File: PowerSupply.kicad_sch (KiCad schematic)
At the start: 8 parts, among them U1201 TPSM365R6FRDNR

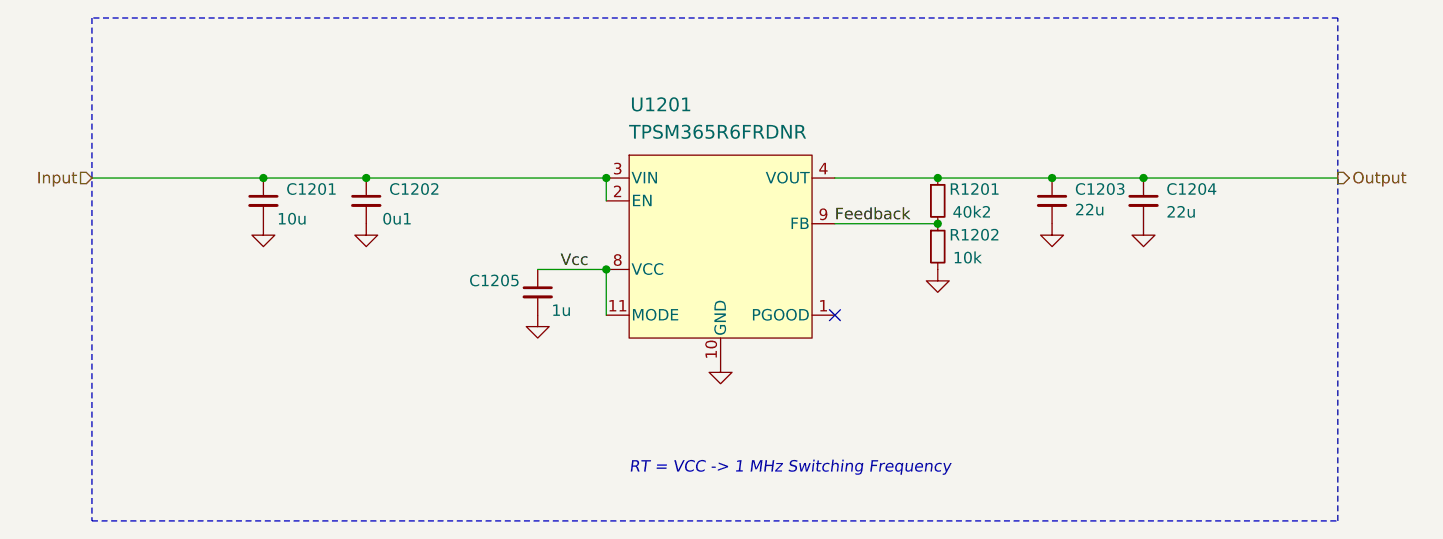
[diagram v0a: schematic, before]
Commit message: Replace step-down
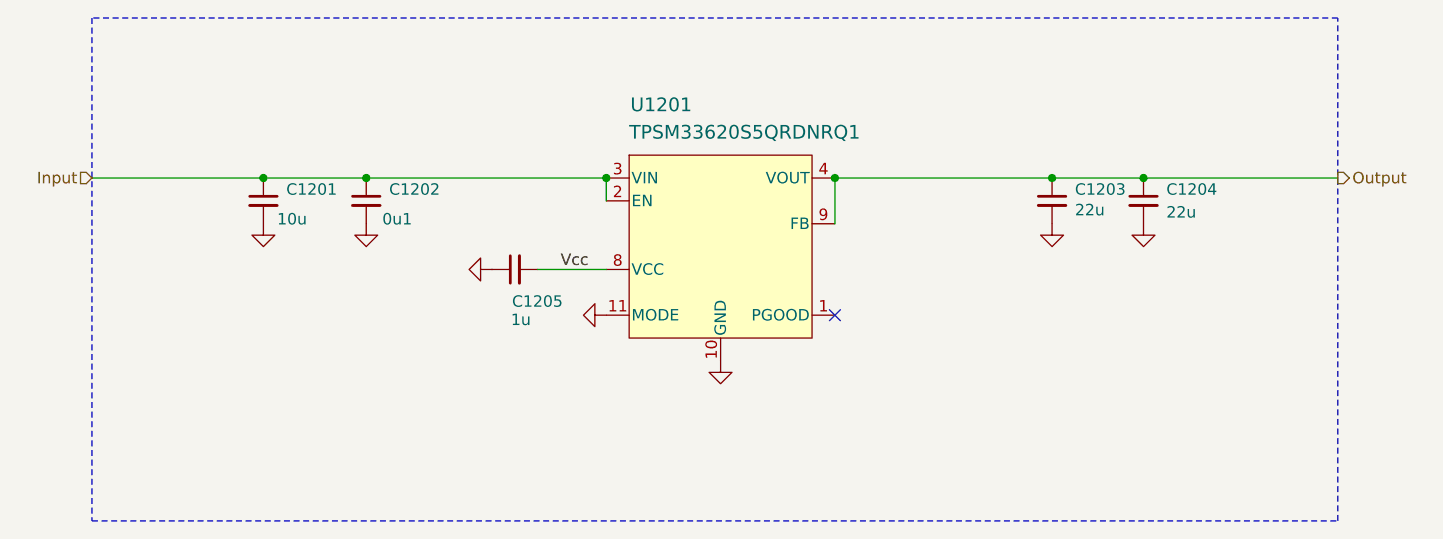
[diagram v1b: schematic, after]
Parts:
- removed R1201: 40k2, V2_Resistor_SMD:R_0603, symbol V2_Resistor:0603_40k2
- removed R1202: 10k, V2_Resistor_SMD:R_0603, symbol V2_Resistor:0603_10k
- U1201: value TPSM365R6FRDNR -> TPSM33620S5QRDNRQ1; symbol V2_Converter_DCDC:TPSM365R6FRDNR -> V2_Converter_DCDC:TPSM33620S5QRDNRQ1; Mouser 595-TPSM365R6FRDNR -> 595-SM33620S5QRDNRQ1; Product TPSM365R6FRDNR -> TPSM33620S5QRDNRQ1; Rating 600mA -> 2A
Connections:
- net Feedback is gone; now on net Output: U1201.9 (FB)
- net GND: now also C1205.1, U1201.11 (MODE); no longer C1205.2
- net Vcc: now also C1205.2; no longer C1205.1, U1201.11 (MODE)
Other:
- note removed: "RT = VCC -> 1 MHz Switching Frequency"
- moved on the sheet: C1205

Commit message: Update
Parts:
- C1201, C1202, C1203, C1204, C1205: Id (none) -> Capacitor:${SYMBOL_NAME}
- U1201: Id (none) -> DCDC:${SYMBOL_NAME}
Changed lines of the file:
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@@
+			)
+		)
+		(property "Id" "DCDC:${SYMBOL_NAME}"
+			(at 148.59 147.32 0)
+			(hide yes)
+			(show_name no)
+			(do_not_autoplace no)
+			(effects
+				(font
+					(size 1.27 1.27)
+				)
 			)
 		)
@@
 			)
 		)
+		(property "Id" "Capacitor:${SYMBOL_NAME}"
+			(at 109.22 113.03 0)
+			(hide yes)
+			(show_name no)
+			(do_not_autoplace no)
+			(effects
+				(font
+					(size 1.27 1.27)
+				)
+			)
+		)
 		(pin "1"
 		)
@@
 			)
 		)
+		(property "Id" "Capacitor:${SYMBOL_NAME}"
+			(at 195.58 113.03 0)
+			(hide yes)
+			(show_name no)
+			(do_not_autoplace no)
+			(effects
+				(font
+					(size 1.27 1.27)
+				)
+			)
+		)
 		(pin "1"
 		)
@@
 			)
 		)
+		(property "Id" "Capacitor:${SYMBOL_NAME}"
+			(at 140.97 105.41 0)
+			(hide yes)
+			(show_name no)
+			(do_not_autoplace no)
+			(effects
+				(font
+					(size 1.27 1.27)
+				)
+			)
+		)
 		(pin "1"
 		)
@@
 			)
 		)
+		(property "Id" "Capacitor:${SYMBOL_NAME}"
+			(at 185.42 113.03 0)
+			(hide yes)
+			(show_name no)
+			(do_not_autoplace no)
+			(effects
+				(font
+					(size 1.27 1.27)
+				)
+			)
+		)
 		(pin "1"
 		)
@@
 			(hide yes)
 			(show_name no)
+			(do_not_autoplace no)
+			(effects
+				(font
+					(size 1.27 1.27)
+				)
+			)
+		)
+		(property "Id" "Capacitor:${SYMBOL_NAME}"
+			(at 97.79 113.03 0)
+			(hide yes)
+			(show_name no)

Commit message: Update
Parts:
- renumbered C1201 to C601, C1202 to C602, C1205 to C603, C1203 to C604, C1204 to C605, U1201 to U601
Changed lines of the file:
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@@
 		(rev "2026-03-28")
 		(company "Versio Duo")
+		(comment 1 "V2 Link Connector")
 	)
 	(junction
@@
 		(in_pos_files yes)
 		(dnp no)
-		(property "Reference" "U1201"
+		(property "Reference" "U601"
 			(at 141.986 87.122 0)
 			(show_name no)
@@
 			(project "connect"
 				(path "/6c8448b4-b04d-47e1-934e-e40cbe27a7be/095cddf1-6522-4d3b-885d-b21acd91d0c6"
-					(reference "U1201")
+					(reference "U601")
 					(unit 1)
 				)
@@
 		(in_pos_files yes)
 		(dnp no)
-		(property "Reference" "C1202"
+		(property "Reference" "C602"
 			(at 111.76 96.52 0)
 			(show_name no)
@@
 			(project "connect"
 				(path "/6c8448b4-b04d-47e1-934e-e40cbe27a7be/095cddf1-6522-4d3b-885d-b21acd91d0c6"
-					(reference "C1202")
+					(reference "C602")
 					(unit 1)
 				)
@@
 		(in_pos_files yes)
 		(dnp no)
-		(property "Reference" "C1204"
+		(property "Reference" "C605"
 			(at 198.12 96.52 0)
 			(show_name no)
@@
 			(project "connect"
 				(path "/6c8448b4-b04d-47e1-934e-e40cbe27a7be/095cddf1-6522-4d3b-885d-b21acd91d0c6"
-					(reference "C1204")
+					(reference "C605")
 					(unit 1)
 				)
@@
 		(in_pos_files yes)
 		(dnp no)
-		(property "Reference" "#PWR1203"
+		(property "Reference" "#PWR0606"
 			(at 185.42 106.68 0)
 			(hide yes)
@@
 			(project "connect"
 				(path "/6c8448b4-b04d-47e1-934e-e40cbe27a7be/095cddf1-6522-4d3b-885d-b21acd91d0c6"
-					(reference "#PWR1203")
+					(reference "#PWR0606")
 					(unit 1)
 				)
@@
 		(in_pos_files yes)
 		(dnp no)
-		(property "Reference" "#PWR1204"
+		(property "Reference" "#PWR0607"
 			(at 195.58 106.68 0)
 			(hide yes)
@@
 			(project "connect"
 				(path "/6c8448b4-b04d-47e1-934e-e40cbe27a7be/095cddf1-6522-4d3b-885d-b21acd91d0c6"
-					(reference "#PWR1204")
+					(reference "#PWR0607")
 					(unit 1)
 				)
@@
 		(in_pos_files yes)
 		(dnp no)
-		(property "Reference" "#PWR1201"
+		(property "Reference" "#PWR0601"
 			(at 97.79 106.68 0)
 			(hide yes)
@@
 			(project "connect"
 				(path "/6c8448b4-b04d-47e1-934e-e40cbe27a7be/095cddf1-6522-4d3b-885d-b21acd91d0c6"
-					(reference "#PWR1201")
+					(reference "#PWR0601")
 					(unit 1)
 				)
@@
 		(in_pos_files yes)
 		(dnp no)
-		(property "Reference" "#PWR1202"
+		(property "Reference" "#PWR0602"
 			(at 109.22 106.68 0)
 			(hide yes)
@@
 			(project "connect"
 				(path "/6c8448b4-b04d-47e1-934e-e40cbe27a7be/095cddf1-6522-4d3b-885d-b21acd91d0c6"
-					(reference "#PWR1202")
+					(reference "#PWR0602")
 					(unit 1)
 				)
@@
 		(in_pos_files yes)
 		(dnp no)
-		(property "Reference" "C1205"
+		(property "Reference" "C603"
 			(at 131.064 108.966 90)
 			(show_name no)
@@
 			(project "connect"
 				(path "/6c8448b4-b04d-47e1-934e-e40cbe27a7be/095cddf1-6522-4d3b-885d-b21acd91d0c6"
-					(reference "C1205")
+					(reference "C603")
 					(unit 1)
 				)
@@
 		(in_pos_files yes)
 		(dnp no)
-		(property "Reference" "C1203"
+		(property "Reference" "C604"
 			(at 187.96 96.52 0)
 			(show_name no)
@@
 			(project "connect"
 				(path "/6c8448b4-b04d-47e1-934e-e40cbe27a7be/095cddf1-6522-4d3b-885d-b21acd91d0c6"
-					(reference "C1203")
+					(reference "C604")
 					(unit 1)
 				)
@@
 		(in_pos_files yes)
 		(dnp no)
-		(property "Reference" "#PWR1206"
+		(property "Reference" "#PWR0603"
 			(at 116.84 105.41 0)
 			(hide yes)
@@
 			(project "connect"
 				(path "/6c8448b4-b04d-47e1-934e-e40cbe27a7be/095cddf1-6522-4d3b-885d-b21acd91d0c6"
-					(reference "#PWR1206")
+					(reference "#PWR0603")
 					(unit 1)
 				)
@@
 		(in_pos_files yes)
 		(dnp no)
-		(property "Reference" "#PWR1208"
+		(property "Reference" "#PWR0604"
 			(at 129.54 110.49 0)
 			(hide yes)
@@
 			(project "connect"
 				(path "/6c8448b4-b04d-47e1-934e-e40cbe27a7be/095cddf1-6522-4d3b-885d-b21acd91d0c6"
-					(reference "#PWR1208")
+					(reference "#PWR0604")
 					(unit 1)
 				)
@@
 		(in_pos_files yes)
 		(dnp no)
-		(property "Reference" "#PWR1207"
+		(property "Reference" "#PWR0605"
 			(at 148.59 121.92 0)
 			(hide yes)
@@
 			(project "connect"
 				(path "/6c8448b4-b04d-47e1-934e-e40cbe27a7be/095cddf1-6522-4d3b-885d-b21acd91d0c6"
-					(reference "#PWR1207")
+					(reference "#PWR0605")
 					(unit 1)
 				)
@@
 		(in_pos_files yes)
 		(dnp no)
-		(property "Reference" "C1201"
+		(property "Reference" "C601"
 			(at 100.33 96.52 0)
 			(show_name no)
@@
 			(project "connect"
 				(path "/6c8448b4-b04d-47e1-934e-e40cbe27a7be/095cddf1-6522-4d3b-885d-b21acd91d0c6"
-					(reference "C1201")
+					(reference "C601")
 					(unit 1)
 				)
